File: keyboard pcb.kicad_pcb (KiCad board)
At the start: 2 copper layers, 0 parts

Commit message: Various changes
Mostly done i think
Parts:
- added C1: 10pF, Capacitor_SMD:C_0603_1608Metric, B.Cu at (351.5, 80.1)
- added C2: 10pF, Capacitor_SMD:C_0603_1608Metric, B.Cu at (345.7, 80.1)
- added C3: 1uF, Capacitor_SMD:C_0603_1608Metric, B.Cu at (359.4, 71.9)
- added C4: 0.1uF, Capacitor_SMD:C_0603_1608Metric, B.Cu at (341.0, 77.3)
- added C5: 0.1uF, Capacitor_SMD:C_0603_1608Metric, B.Cu at (339.0, 67.2)
- added C6: 0.1uF, Capacitor_SMD:C_0603_1608Metric, B.Cu at (325.9, 69.3)
- added C7: 0.1uF, Capacitor_SMD:C_0603_1608Metric, B.Cu at (329.7, 65.4)
- added C8: 1uF, Capacitor_SMD:C_0603_1608Metric, B.Cu at (361.1, 66.3)
- added D1: SOD-123, random-keyboard-parts:D_SOD-123-Pretty, B.Cu at (59.1, 101.5)
- added D10: SOD-123, random-keyboard-parts:D_SOD-123-Pretty, B.Cu at (78.3, 158.8)
- added D100: SOD-123, random-keyboard-parts:D_SOD-123-Pretty, B.Cu at (363.9, 158.7)
- added D101: SOD-123, random-keyboard-parts:D_SOD-123-Pretty, B.Cu at (363.9, 177.8)
- added D102: SOD-123, random-keyboard-parts:D_SOD-123-Pretty, B.Cu at (363.8, 196.8)
- added D11: SOD-123, random-keyboard-parts:D_SOD-123-Pretty, B.Cu at (78.3, 177.8)
- added D12: SOD-123, random-keyboard-parts:D_SOD-123-Pretty, B.Cu at (78.1, 196.8)
- added D13: SOD-123, random-keyboard-parts:D_SOD-123-Pretty, B.Cu at (97.2, 101.5)
- added D14: SOD-123, random-keyboard-parts:D_SOD-123-Pretty, B.Cu at (97.3, 120.8)
- added D15: SOD-123, random-keyboard-parts:D_SOD-123-Pretty, B.Cu at (97.2, 139.6)
- added D16: SOD-123, random-keyboard-parts:D_SOD-123-Pretty, B.Cu at (97.2, 158.7)
- added D17: SOD-123, random-keyboard-parts:D_SOD-123-Pretty, B.Cu at (97.1, 177.8)
- added D18: SOD-123, random-keyboard-parts:D_SOD-123-Pretty, B.Cu at (97.2, 196.7)
- added D19: SOD-123, random-keyboard-parts:D_SOD-123-Pretty, B.Cu at (116.3, 101.5)
- added D2: SOD-123, random-keyboard-parts:D_SOD-123-Pretty, B.Cu at (59.1, 120.5)
- added D20: SOD-123, random-keyboard-parts:D_SOD-123-Pretty, B.Cu at (116.2, 120.6)
- added D21: SOD-123, random-keyboard-parts:D_SOD-123-Pretty, B.Cu at (116.2, 139.6)
- added D22: SOD-123, random-keyboard-parts:D_SOD-123-Pretty, B.Cu at (116.2, 158.7)
- added D23: SOD-123, random-keyboard-parts:D_SOD-123-Pretty, B.Cu at (116.2, 177.7)
- added D24: SOD-123, random-keyboard-parts:D_SOD-123-Pretty, B.Cu at (116.2, 196.8)
- added D25: SOD-123, random-keyboard-parts:D_SOD-123-Pretty, B.Cu at (135.3, 101.5)
- added D26: SOD-123, random-keyboard-parts:D_SOD-123-Pretty, B.Cu at (135.3, 120.6)
- added D27: SOD-123, random-keyboard-parts:D_SOD-123-Pretty, B.Cu at (135.3, 139.6)
- added D28: SOD-123, random-keyboard-parts:D_SOD-123-Pretty, B.Cu at (135.3, 158.7)
- added D29: SOD-123, random-keyboard-parts:D_SOD-123-Pretty, B.Cu at (135.3, 177.7)
- added D3: SOD-123, random-keyboard-parts:D_SOD-123-Pretty, B.Cu at (58.9, 139.8)
- added D30: SOD-123, random-keyboard-parts:D_SOD-123-Pretty, B.Cu at (135.4, 196.9)
- added D31: SOD-123, random-keyboard-parts:D_SOD-123-Pretty, B.Cu at (154.3, 101.5)
- added D32: SOD-123, random-keyboard-parts:D_SOD-123-Pretty, B.Cu at (154.4, 120.6)
- added D33: SOD-123, random-keyboard-parts:D_SOD-123-Pretty, B.Cu at (154.4, 139.6)
- added D34: SOD-123, random-keyboard-parts:D_SOD-123-Pretty, B.Cu at (154.3, 158.6)
- added D35: SOD-123, random-keyboard-parts:D_SOD-123-Pretty, B.Cu at (154.3, 177.8)
- added D36: SOD-123, random-keyboard-parts:D_SOD-123-Pretty, B.Cu at (154.3, 196.8)
- added D37: SOD-123, random-keyboard-parts:D_SOD-123-Pretty, B.Cu at (173.4, 101.5)
- added D38: SOD-123, random-keyboard-parts:D_SOD-123-Pretty, B.Cu at (173.4, 120.6)
- added D39: SOD-123, random-keyboard-parts:D_SOD-123-Pretty, B.Cu at (173.4, 139.6)
- added D4: SOD-123, random-keyboard-parts:D_SOD-123-Pretty, B.Cu at (58.9, 158.7)
- added D40: SOD-123, random-keyboard-parts:D_SOD-123-Pretty, B.Cu at (173.3, 158.7)
- added D41: SOD-123, random-keyboard-parts:D_SOD-123-Pretty, B.Cu at (173.4, 177.8)
- added D42: SOD-123, random-keyboard-parts:D_SOD-123-Pretty, B.Cu at (173.5, 196.9)
- added D43: SOD-123, random-keyboard-parts:D_SOD-123-Pretty, B.Cu at (192.4, 101.6)
- added D44: SOD-123, random-keyboard-parts:D_SOD-123-Pretty, B.Cu at (192.4, 120.6)
- added D45: SOD-123, random-keyboard-parts:D_SOD-123-Pretty, B.Cu at (192.4, 139.7)
- added D46: SOD-123, random-keyboard-parts:D_SOD-123-Pretty, B.Cu at (192.4, 158.7)
- added D47: SOD-123, random-keyboard-parts:D_SOD-123-Pretty, B.Cu at (192.4, 177.8)
- added D48: SOD-123, random-keyboard-parts:D_SOD-123-Pretty, B.Cu at (192.4, 196.8)
- added D49: SOD-123, random-keyboard-parts:D_SOD-123-Pretty, B.Cu at (211.5, 101.5)
- added D5: SOD-123, random-keyboard-parts:D_SOD-123-Pretty, B.Cu at (58.9, 177.7)
- added D50: SOD-123, random-keyboard-parts:D_SOD-123-Pretty, B.Cu at (211.5, 120.6)
- added D51: SOD-123, random-keyboard-parts:D_SOD-123-Pretty, B.Cu at (211.5, 139.8)
- added D52: SOD-123, random-keyboard-parts:D_SOD-123-Pretty, B.Cu at (211.4, 158.7)
- added D53: SOD-123, random-keyboard-parts:D_SOD-123-Pretty, B.Cu at (211.5, 177.7)
- added D54: SOD-123, random-keyboard-parts:D_SOD-123-Pretty, B.Cu at (211.5, 196.8)
- added D55: SOD-123, random-keyboard-parts:D_SOD-123-Pretty, B.Cu at (230.5, 101.6)
- added D56: SOD-123, random-keyboard-parts:D_SOD-123-Pretty, B.Cu at (230.5, 120.6)
- added D57: SOD-123, random-keyboard-parts:D_SOD-123-Pretty, B.Cu at (230.5, 139.6)
- added D58: SOD-123, random-keyboard-parts:D_SOD-123-Pretty, B.Cu at (230.5, 158.7)
- added D59: SOD-123, random-keyboard-parts:D_SOD-123-Pretty, B.Cu at (230.5, 177.7)
- added D6: SOD-123, random-keyboard-parts:D_SOD-123-Pretty, B.Cu at (59.2, 196.8)
- added D60: SOD-123, random-keyboard-parts:D_SOD-123-Pretty, B.Cu at (230.6, 196.7)
- added D61: SOD-123, random-keyboard-parts:D_SOD-123-Pretty, B.Cu at (249.6, 101.5)
- added D62: SOD-123, random-keyboard-parts:D_SOD-123-Pretty, B.Cu at (249.6, 120.6)
- added D63: SOD-123, random-keyboard-parts:D_SOD-123-Pretty, B.Cu at (249.6, 139.7)
- added D64: SOD-123, random-keyboard-parts:D_SOD-123-Pretty, B.Cu at (249.6, 158.7)
- added D65: SOD-123, random-keyboard-parts:D_SOD-123-Pretty, B.Cu at (249.6, 177.8)
- added D66: SOD-123, random-keyboard-parts:D_SOD-123-Pretty, B.Cu at (249.6, 196.7)
- added D67: SOD-123, random-keyboard-parts:D_SOD-123-Pretty, B.Cu at (268.6, 101.6)
- added D68: SOD-123, random-keyboard-parts:D_SOD-123-Pretty, B.Cu at (268.6, 120.6)
- added D69: SOD-123, random-keyboard-parts:D_SOD-123-Pretty, B.Cu at (268.6, 139.7)
- added D7: SOD-123, random-keyboard-parts:D_SOD-123-Pretty, B.Cu at (78.1, 101.7)
- added D70: SOD-123, random-keyboard-parts:D_SOD-123-Pretty, B.Cu at (268.6, 158.7)
- added D71: SOD-123, random-keyboard-parts:D_SOD-123-Pretty, B.Cu at (268.6, 177.8)
- added D72: SOD-123, random-keyboard-parts:D_SOD-123-Pretty, B.Cu at (268.5, 196.7)
- added D73: SOD-123, random-keyboard-parts:D_SOD-123-Pretty, B.Cu at (287.8, 101.6)
- added D74: SOD-123, random-keyboard-parts:D_SOD-123-Pretty, B.Cu at (287.7, 120.6)
- added D75: SOD-123, random-keyboard-parts:D_SOD-123-Pretty, B.Cu at (287.7, 139.7)
- added D76: SOD-123, random-keyboard-parts:D_SOD-123-Pretty, B.Cu at (287.7, 158.7)
- added D77: SOD-123, random-keyboard-parts:D_SOD-123-Pretty, B.Cu at (287.7, 177.8)
- added D78: SOD-123, random-keyboard-parts:D_SOD-123-Pretty, B.Cu at (287.7, 196.8)
- added D79: SOD-123, random-keyboard-parts:D_SOD-123-Pretty, B.Cu at (306.7, 101.6)
- added D8: SOD-123, random-keyboard-parts:D_SOD-123-Pretty, B.Cu at (78.2, 120.7)
- added D80: SOD-123, random-keyboard-parts:D_SOD-123-Pretty, B.Cu at (306.7, 120.6)
- added D81: SOD-123, random-keyboard-parts:D_SOD-123-Pretty, B.Cu at (306.7, 139.7)
- added D82: SOD-123, random-keyboard-parts:D_SOD-123-Pretty, B.Cu at (306.7, 158.7)
- added D83: SOD-123, random-keyboard-parts:D_SOD-123-Pretty, B.Cu at (306.7, 177.8)
- added D84: SOD-123, random-keyboard-parts:D_SOD-123-Pretty, B.Cu at (306.8, 196.9)
- added D85: SOD-123, random-keyboard-parts:D_SOD-123-Pretty, B.Cu at (325.8, 101.5)
- added D86: SOD-123, random-keyboard-parts:D_SOD-123-Pretty, B.Cu at (325.8, 120.6)
- added D87: SOD-123, random-keyboard-parts:D_SOD-123-Pretty, B.Cu at (325.8, 139.8)
- added D88: SOD-123, random-keyboard-parts:D_SOD-123-Pretty, B.Cu at (325.8, 158.7)
- added D89: SOD-123, random-keyboard-parts:D_SOD-123-Pretty, B.Cu at (325.8, 177.7)
- added D9: SOD-123, random-keyboard-parts:D_SOD-123-Pretty, B.Cu at (78.2, 139.8)
- added D90: SOD-123, random-keyboard-parts:D_SOD-123-Pretty, B.Cu at (325.7, 196.8)
- added D91: SOD-123, random-keyboard-parts:D_SOD-123-Pretty, B.Cu at (344.8, 101.5)
- added D92: SOD-123, random-keyboard-parts:D_SOD-123-Pretty, B.Cu at (344.8, 120.6)
- added D93: SOD-123, random-keyboard-parts:D_SOD-123-Pretty, B.Cu at (344.8, 139.6)
- added D94: SOD-123, random-keyboard-parts:D_SOD-123-Pretty, B.Cu at (344.8, 158.7)
- added D95: SOD-123, random-keyboard-parts:D_SOD-123-Pretty, B.Cu at (344.8, 177.7)
- added D96: SOD-123, random-keyboard-parts:D_SOD-123-Pretty, B.Cu at (344.8, 196.8)
- added D97: SOD-123, random-keyboard-parts:D_SOD-123-Pretty, B.Cu at (363.9, 101.6)
- added D98: SOD-123, random-keyboard-parts:D_SOD-123-Pretty, B.Cu at (363.9, 120.6)
- added D99: SOD-123, random-keyboard-parts:D_SOD-123-Pretty, B.Cu at (363.9, 139.7)
- added F1: 500mA, Fuse:Fuse_1206_3216Metric, B.Cu at (361.0, 63.5)
- added J1: RGB, Connector_PinHeader_1.00mm:PinHeader_1x03_P1.00mm_Vertical, B.Cu at (355.9, 85.3)
- added J10: OLED, Connector_PinHeader_1.00mm:PinHeader_1x04_P1.00mm_Vertical, B.Cu at (345.8, 85.3)
- added J11: F, Connector_PinHeader_1.00mm:PinHeader_1x08_P1.00mm_Vertical, B.Cu at (327.9, 62.2)
- added J12: B, Connector_PinHeader_1.00mm:PinHeader_1x08_P1.00mm_Vertical, B.Cu at (336.9, 62.2)
- added J13: D, Connector_PinHeader_1.00mm:PinHeader_1x08_P1.00mm_Vertical, B.Cu at (341.0, 82.9)
- added J14: USB_C_Receptacle_USB2.0, Connector_USB:USB_C_Receptacle_HRO_TYPE-C-31-M-12, B.Cu at (352.7, 65.3)
- added J2: E, Connector_PinHeader_1.00mm:PinHeader_1x02_P1.00mm_Vertical, B.Cu at (331.0, 82.9)
- added J3: A, Connector_PinHeader_1.00mm:PinHeader_1x04_P1.00mm_Vertical, B.Cu at (324.0, 71.4)
- added J4: Encoder, Connector_PinHeader_1.00mm:PinHeader_1x05_P1.00mm_Vertical, B.Cu at (351.9, 85.3)
- added J5: E, Connector_PinHeader_1.00mm:PinHeader_1x01_P1.00mm_Vertical, B.Cu at (323.0, 78.7)
- added J6: C, Connector_PinHeader_1.00mm:PinHeader_1x08_P1.00mm_Vertical, B.Cu at (328.9, 82.9)
- added J7: E, Connector_PinHeader_1.00mm:PinHeader_1x02_P1.00mm_Vertical, B.Cu at (345.8, 71.4)
- added J8: A, Connector_PinHeader_1.00mm:PinHeader_1x04_P1.00mm_Vertical, B.Cu at (324.0, 73.7)
- added J9: E, Connector_PinHeader_1.00mm:PinHeader_1x02_P1.00mm_Vertical, B.Cu at (334.9, 62.2)
- added JP1: 5, Jumper:SolderJumper-3_P1.3mm_Bridged12_Pad1.0x1.5mm_NumberLabels, B.Cu at (361.2, 69.0)
- added LED1: PWR, LED_SMD:LED_0201_0603Metric, B.Cu at (353.3, 77.7)
- added LED2: Yellow, LED_SMD:LED_0201_0603Metric, B.Cu at (321.3, 77.1)
- added MX1: MX-NoLED, MX_Only:MXOnly-1U-Hotswap-Antishear, F.Cu at (50.8, 101.6)
- added MX10: MX-NoLED, MX_Only:MXOnly-1U-Hotswap-Antishear, F.Cu at (69.8, 158.8)
- added MX100: MX-NoLED, MX_Only:MXOnly-1U-Hotswap-Antishear, F.Cu at (355.6, 158.8)
- added MX101: MX-NoLED, MX_Only:MXOnly-1U-Hotswap-Antishear, F.Cu at (355.6, 177.8)
- added MX102: MX-NoLED, MX_Only:MXOnly-1U-Hotswap-Antishear, F.Cu at (355.6, 196.8)
- added MX11: MX-NoLED, MX_Only:MXOnly-1U-Hotswap-Antishear, F.Cu at (69.8, 177.8)
- added MX12: MX-NoLED, MX_Only:MXOnly-1U-Hotswap-Antishear, F.Cu at (69.8, 196.8)
- added MX13: MX-NoLED, MX_Only:MXOnly-1U-Hotswap-Antishear, F.Cu at (88.9, 101.6)
- added MX14: MX-NoLED, MX_Only:MXOnly-1U-Hotswap-Antishear, F.Cu at (88.9, 120.7)
- added MX15: MX-NoLED, MX_Only:MXOnly-1U-Hotswap-Antishear, F.Cu at (88.9, 139.7)
- added MX16: MX-NoLED, MX_Only:MXOnly-1U-Hotswap-Antishear, F.Cu at (88.9, 158.8)
- added MX17: MX-NoLED, MX_Only:MXOnly-1U-Hotswap-Antishear, F.Cu at (88.9, 177.8)
- added MX18: MX-NoLED, MX_Only:MXOnly-1U-Hotswap-Antishear, F.Cu at (88.9, 196.8)
- added MX19: MX-NoLED, MX_Only:MXOnly-1U-Hotswap-Antishear, F.Cu at (108.0, 101.6)
- added MX2: MX-NoLED, MX_Only:MXOnly-1U-Hotswap-Antishear, F.Cu at (50.8, 120.7)
- added MX20: MX-NoLED, MX_Only:MXOnly-1U-Hotswap-Antishear, F.Cu at (108.0, 120.7)
- added MX21: MX-NoLED, MX_Only:MXOnly-1U-Hotswap-Antishear, F.Cu at (108.0, 139.7)
- added MX22: MX-NoLED, MX_Only:MXOnly-1U-Hotswap-Antishear, F.Cu at (108.0, 158.8)
- added MX23: MX-NoLED, MX_Only:MXOnly-1U-Hotswap-Antishear, F.Cu at (108.0, 177.8)
- added MX24: MX-NoLED, MX_Only:MXOnly-1U-Hotswap-Antishear, F.Cu at (108.0, 196.8)
- added MX25: MX-NoLED, MX_Only:MXOnly-1U-Hotswap-Antishear, F.Cu at (127.0, 101.6)
- added MX26: MX-NoLED, MX_Only:MXOnly-1U-Hotswap-Antishear, F.Cu at (127.0, 120.7)
- added MX27: MX-NoLED, MX_Only:MXOnly-1U-Hotswap-Antishear, F.Cu at (127.0, 139.7)
- added MX28: MX-NoLED, MX_Only:MXOnly-1U-Hotswap-Antishear, F.Cu at (127.0, 158.8)
- added MX29: MX-NoLED, MX_Only:MXOnly-1U-Hotswap-Antishear, F.Cu at (127.0, 177.8)
- added MX3: MX-NoLED, MX_Only:MXOnly-1U-Hotswap-Antishear, F.Cu at (50.8, 139.7)
- added MX30: MX-NoLED, MX_Only:MXOnly-1U-Hotswap-Antishear, F.Cu at (127.0, 196.8)
- added MX31: MX-NoLED, MX_Only:MXOnly-1U-Hotswap-Antishear, F.Cu at (146.1, 101.6)
- added MX32: MX-NoLED, MX_Only:MXOnly-1U-Hotswap-Antishear, F.Cu at (146.1, 120.7)
- added MX33: MX-NoLED, MX_Only:MXOnly-1U-Hotswap-Antishear, F.Cu at (146.1, 139.7)
- added MX34: MX-NoLED, MX_Only:MXOnly-1U-Hotswap-Antishear, F.Cu at (146.1, 158.8)
- added MX35: MX-NoLED, MX_Only:MXOnly-1U-Hotswap-Antishear, F.Cu at (146.1, 177.8)
- added MX36: MX-NoLED, MX_Only:MXOnly-1U-Hotswap-Antishear, F.Cu at (146.1, 196.8)
- added MX37: MX-NoLED, MX_Only:MXOnly-1U-Hotswap-Antishear, F.Cu at (165.1, 101.6)
- added MX38: MX-NoLED, MX_Only:MXOnly-1U-Hotswap-Antishear, F.Cu at (165.1, 120.7)
- added MX39: MX-NoLED, MX_Only:MXOnly-1U-Hotswap-Antishear, F.Cu at (165.1, 139.7)
- added MX4: MX-NoLED, MX_Only:MXOnly-1U-Hotswap-Antishear, F.Cu at (50.8, 158.8)
- added MX40: MX-NoLED, MX_Only:MXOnly-1U-Hotswap-Antishear, F.Cu at (165.1, 158.8)
- added MX41: MX-NoLED, MX_Only:MXOnly-1U-Hotswap-Antishear, F.Cu at (165.1, 177.8)
- added MX42: MX-NoLED, MX_Only:MXOnly-1U-Hotswap-Antishear, F.Cu at (165.1, 196.8)
- added MX43: MX-NoLED, MX_Only:MXOnly-1U-Hotswap-Antishear, F.Cu at (184.2, 101.6)
- added MX44: MX-NoLED, MX_Only:MXOnly-1U-Hotswap-Antishear, F.Cu at (184.2, 120.7)
- added MX45: MX-NoLED, MX_Only:MXOnly-1U-Hotswap-Antishear, F.Cu at (184.2, 139.7)
- added MX46: MX-NoLED, MX_Only:MXOnly-1U-Hotswap-Antishear, F.Cu at (184.2, 158.8)
- added MX47: MX-NoLED, MX_Only:MXOnly-1U-Hotswap-Antishear, F.Cu at (184.2, 177.8)
- added MX48: MX-NoLED, MX_Only:MXOnly-1U-Hotswap-Antishear, F.Cu at (184.2, 196.8)
- added MX49: MX-NoLED, MX_Only:MXOnly-1U-Hotswap-Antishear, F.Cu at (203.2, 101.6)
- added MX5: MX-NoLED, MX_Only:MXOnly-1U-Hotswap-Antishear, F.Cu at (50.8, 177.8)
- added MX50: MX-NoLED, MX_Only:MXOnly-1U-Hotswap-Antishear, F.Cu at (203.2, 120.7)
- added MX51: MX-NoLED, MX_Only:MXOnly-1U-Hotswap-Antishear, F.Cu at (203.2, 139.7)
- added MX52: MX-NoLED, MX_Only:MXOnly-1U-Hotswap-Antishear, F.Cu at (203.2, 158.8)
- added MX53: MX-NoLED, MX_Only:MXOnly-1U-Hotswap-Antishear, F.Cu at (203.2, 177.8)
- added MX54: MX-NoLED, MX_Only:MXOnly-1U-Hotswap-Antishear, F.Cu at (203.2, 196.8)
- added MX55: MX-NoLED, MX_Only:MXOnly-1U-Hotswap-Antishear, F.Cu at (222.2, 101.6)
- added MX56: MX-NoLED, MX_Only:MXOnly-1U-Hotswap-Antishear, F.Cu at (222.2, 120.7)
- added MX57: MX-NoLED, MX_Only:MXOnly-1U-Hotswap-Antishear, F.Cu at (222.2, 139.7)
- added MX58: MX-NoLED, MX_Only:MXOnly-1U-Hotswap-Antishear, F.Cu at (222.2, 158.8)
- added MX59: MX-NoLED, MX_Only:MXOnly-1U-Hotswap-Antishear, F.Cu at (222.2, 177.8)
- added MX6: MX-NoLED, MX_Only:MXOnly-1U-Hotswap-Antishear, F.Cu at (50.8, 196.8)
- added MX60: MX-NoLED, MX_Only:MXOnly-1U-Hotswap-Antishear, F.Cu at (222.2, 196.8)
- added MX61: MX-NoLED, MX_Only:MXOnly-1U-Hotswap-Antishear, F.Cu at (241.3, 101.6)
- added MX62: MX-NoLED, MX_Only:MXOnly-1U-Hotswap-Antishear, F.Cu at (241.3, 120.7)
- added MX63: MX-NoLED, MX_Only:MXOnly-1U-Hotswap-Antishear, F.Cu at (241.3, 139.7)
- added MX64: MX-NoLED, MX_Only:MXOnly-1U-Hotswap-Antishear, F.Cu at (241.3, 158.8)
- added MX65: MX-NoLED, MX_Only:MXOnly-1U-Hotswap-Antishear, F.Cu at (241.3, 177.8)
- added MX66: MX-NoLED, MX_Only:MXOnly-1U-Hotswap-Antishear, F.Cu at (241.3, 196.8)
- added MX67: MX-NoLED, MX_Only:MXOnly-1U-Hotswap-Antishear, F.Cu at (260.4, 101.6)
- added MX68: MX-NoLED, MX_Only:MXOnly-1U-Hotswap-Antishear, F.Cu at (260.4, 120.7)
- added MX69: MX-NoLED, MX_Only:MXOnly-1U-Hotswap-Antishear, F.Cu at (260.4, 139.7)
- added MX7: MX-NoLED, MX_Only:MXOnly-1U-Hotswap-Antishear, F.Cu at (69.8, 101.6)
- added MX70: MX-NoLED, MX_Only:MXOnly-1U-Hotswap-Antishear, F.Cu at (260.4, 158.8)
- added MX71: MX-NoLED, MX_Only:MXOnly-1U-Hotswap-Antishear, F.Cu at (260.4, 177.8)
- added MX72: MX-NoLED, MX_Only:MXOnly-1U-Hotswap-Antishear, F.Cu at (260.4, 196.8)
- added MX73: MX-NoLED, MX_Only:MXOnly-1U-Hotswap-Antishear, F.Cu at (279.4, 101.6)
- added MX74: MX-NoLED, MX_Only:MXOnly-1U-Hotswap-Antishear, F.Cu at (279.4, 120.7)
- added MX75: MX-NoLED, MX_Only:MXOnly-1U-Hotswap-Antishear, F.Cu at (279.4, 139.7)
- added MX76: MX-NoLED, MX_Only:MXOnly-1U-Hotswap-Antishear, F.Cu at (279.4, 158.8)
- added MX77: MX-NoLED, MX_Only:MXOnly-1U-Hotswap-Antishear, F.Cu at (279.4, 177.8)
- added MX78: MX-NoLED, MX_Only:MXOnly-1U-Hotswap-Antishear, F.Cu at (279.4, 196.8)
- added MX79: MX-NoLED, MX_Only:MXOnly-1U-Hotswap-Antishear, F.Cu at (298.4, 101.6)
- added MX8: MX-NoLED, MX_Only:MXOnly-1U-Hotswap-Antishear, F.Cu at (69.8, 120.7)
- added MX80: MX-NoLED, MX_Only:MXOnly-1U-Hotswap-Antishear, F.Cu at (298.4, 120.7)
- added MX81: MX-NoLED, MX_Only:MXOnly-1U-Hotswap-Antishear, F.Cu at (298.4, 139.7)
- added MX82: MX-NoLED, MX_Only:MXOnly-1U-Hotswap-Antishear, F.Cu at (298.4, 158.8)
- added MX83: MX-NoLED, MX_Only:MXOnly-1U-Hotswap-Antishear, F.Cu at (298.4, 177.8)
- added MX84: MX-NoLED, MX_Only:MXOnly-1U-Hotswap-Antishear, F.Cu at (298.4, 196.8)
- added MX85: MX-NoLED, MX_Only:MXOnly-1U-Hotswap-Antishear, F.Cu at (317.5, 101.6)
- added MX86: MX-NoLED, MX_Only:MXOnly-1U-Hotswap-Antishear, F.Cu at (317.5, 120.7)
- added MX87: MX-NoLED, MX_Only:MXOnly-1U-Hotswap-Antishear, F.Cu at (317.5, 139.7)
- added MX88: MX-NoLED, MX_Only:MXOnly-1U-Hotswap-Antishear, F.Cu at (317.5, 158.8)
- added MX89: MX-NoLED, MX_Only:MXOnly-1U-Hotswap-Antishear, F.Cu at (317.5, 177.8)
- added MX9: MX-NoLED, MX_Only:MXOnly-1U-Hotswap-Antishear, F.Cu at (69.8, 139.7)
- added MX90: MX-NoLED, MX_Only:MXOnly-1U-Hotswap-Antishear, F.Cu at (317.5, 196.8)
- added MX91: MX-NoLED, MX_Only:MXOnly-1U-Hotswap-Antishear, F.Cu at (336.6, 101.6)
- added MX92: MX-NoLED, MX_Only:MXOnly-1U-Hotswap-Antishear, F.Cu at (336.6, 120.7)
- added MX93: MX-NoLED, MX_Only:MXOnly-1U-Hotswap-Antishear, F.Cu at (336.6, 139.7)
- added MX94: MX-NoLED, MX_Only:MXOnly-1U-Hotswap-Antishear, F.Cu at (336.6, 158.8)
- added MX95: MX-NoLED, MX_Only:MXOnly-1U-Hotswap-Antishear, F.Cu at (336.6, 177.8)
- added MX96: MX-NoLED, MX_Only:MXOnly-1U-Hotswap-Antishear, F.Cu at (336.6, 196.8)
- added MX97: MX-NoLED, MX_Only:MXOnly-1U-Hotswap-Antishear, F.Cu at (355.6, 101.6)
- added MX98: MX-NoLED, MX_Only:MXOnly-1U-Hotswap-Antishear, F.Cu at (355.6, 120.7)
- added MX99: MX-NoLED, MX_Only:MXOnly-1U-Hotswap-Antishear, F.Cu at (355.6, 139.7)
- added R1: 10k, Resistor_SMD:R_0603_1608Metric, B.Cu at (321.1, 66.9)
- added R2: 1k, Resistor_SMD:R_0603_1608Metric, B.Cu at (324.9, 77.0)
- added R3: 1k, Resistor_SMD:R_0603_1608Metric, B.Cu at (355.5, 78.8)
- added R4: 1k, Resistor_SMD:R_0603_1608Metric, B.Cu at (318.3, 77.1)
- added R5: 22, Resistor_SMD:R_0603_1608Metric, B.Cu at (349.1, 73.5)
- added R6: 22, Resistor_SMD:R_0603_1608Metric, B.Cu at (349.1, 75.1)
- added R7: 5.1k, Resistor_SMD:R_0603_1608Metric, B.Cu at (356.3, 71.3)
- added R8: 5.1k, Resistor_SMD:R_0603_1608Metric, B.Cu at (349.1, 71.5)
- added SW1: RESET, SamacSys_Parts:CMI126601D03, B.Cu at (316.0, 63.5)
- added U1: MCP1825S, Package_TO_SOT_SMD:SOT-223-3_TabPin2, B.Cu at (360.0, 78.7)
- added U2: AT90USB1286-MU, Package_DFN_QFN:QFN-64-1EP_9x9mm_P0.5mm_EP7.5x7.5mm, B.Cu at (333.0, 73.2)
- added U2A1: OP07, Package_SO:SOIC-8_3.9x4.9mm_P1.27mm, B.Cu at (317.2, 80.6)
- added Y1: 16MHz, Crystal:Crystal_SMD_3225-4Pin_3.2x2.5mm, B.Cu at (348.6, 80.1)
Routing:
- net ROW5: track 0.00 -> 518.9 mm, vias 0 -> 10
- net ROW4: track 0.00 -> 498.2 mm, vias 0 -> 10
- net ROW3: track 0.00 -> 440.6 mm, vias 0 -> 6
- net COL0: track 0.00 -> 402.6 mm
- net ROW2: track 0.00 -> 401.0 mm, vias 0 -> 4
- net COL1: track 0.00 -> 383.9 mm
- net COL2: track 0.00 -> 367.2 mm
- net ROW1: track 0.00 -> 364.8 mm, vias 0 -> 2
- net ROW0: track 0.00 -> 354.5 mm
- net COL3: track 0.00 -> 347.0 mm
- net COL4: track 0.00 -> 326.7 mm
- net COL5: track 0.00 -> 308.0 mm
- net COL6: track 0.00 -> 289.4 mm
- net COL7: track 0.00 -> 257.7 mm
- net COL8: track 0.00 -> 238.6 mm
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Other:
- board outline added: 323.9 x 145.3 mm
- net class Default: trace_width 0.25 -> 0.254
- net class Power added: clearance 0.2, trace_width 0.381, via_dia 0.8, via_drill 0.4

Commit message: Touching it up
Added Fillzones and better Silkscreen
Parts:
- removed J3: A, Connector_PinHeader_1.00mm:PinHeader_1x04_P1.00mm_Vertical
- added A: A, Connector_PinHeader_1.00mm:PinHeader_1x04_P1.00mm_Vertical, B.Cu at (324.0, 71.4)
- renumbered J8 to A, J12 to B, J6 to C, J13 to D, J9 to E, J7 to E, J2 to E, J5 to E2, J4 to ENCODER, J11 to F, LED2 to LED, J10 to OLED, LED1 to PWR, SW1 to RESET, J1 to RGB, J14 to USB-C
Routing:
- net GND: vias 9 -> 73
- added copper zone on B.Cu, net GND
- added copper zone on F.Cu, net GND
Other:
- board text added: "A0 A1 A2 A3"
- board text added: "A4 A5 A6 A7"
- board text added: "B7 B6 B5 B4 B3 B2 B1 B0"
- board text added: "C0 C1 C2 C3 C4 C5 C6 C7"
- board text added: "D0 D1 D2 D3 D4 D5 D6 D7"
- board text added: "E0 E1"
- board text added: "E4 E5"
- board text added: "E7 E6"
- board text added: "F0 F1 F2 F3 F4 F5 F6 F7"
- board text added: "GND 5V SCL SDA"
- board text added: "GND 5V SW DT CLK"
- board text added: "GND D 5V"

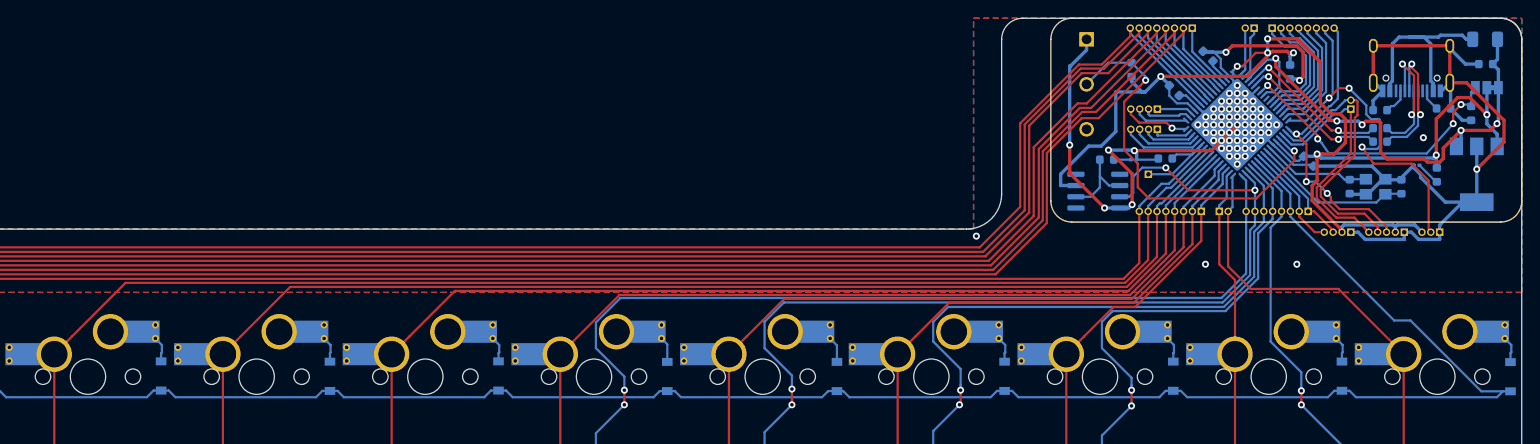
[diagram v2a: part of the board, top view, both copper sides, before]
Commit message: added values for JLCPCB
added field value for JLCPCB
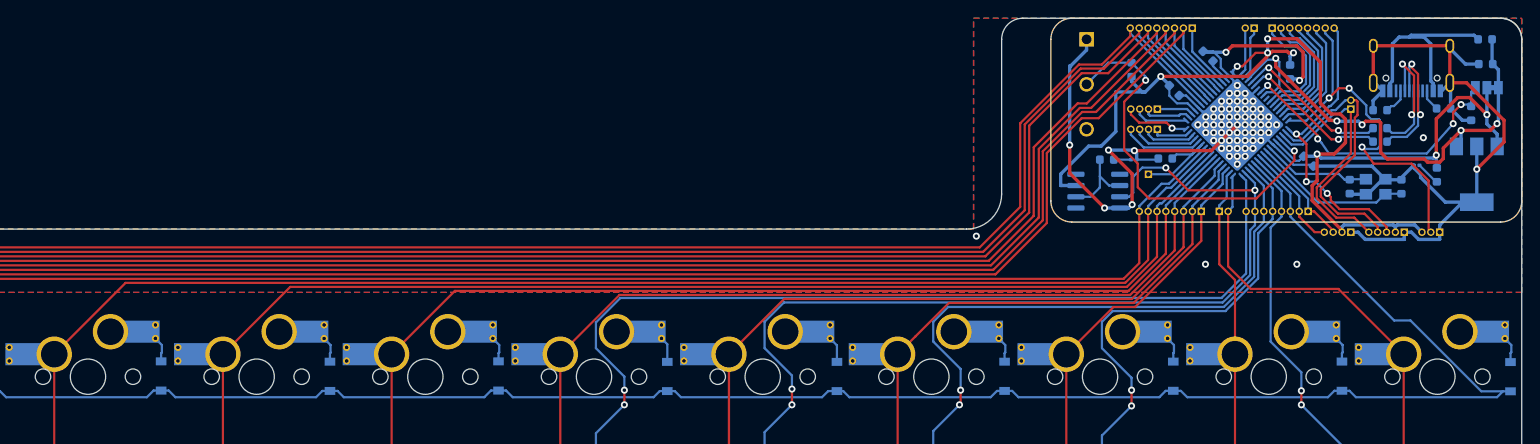
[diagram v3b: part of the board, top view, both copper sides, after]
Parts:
- F1: footprint Fuse:Fuse_1206_3216Metric -> Fuse:Fuse_0603_1608Metric
- renumbered RGB to J1, OLED to J10, F to J11, B to J12, D to J13, USB-C to J14, E to J2, A to J3, ENCODER to J4, E2 to J5, C to J6, E to J7, A to J8, E to J9, PWR to LED1, LED to LED2, RESET to SW1
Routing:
- net Net-(F1-Pad2): track 23.3 -> 23.9 mm
